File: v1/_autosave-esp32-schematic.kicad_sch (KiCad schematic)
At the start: 47 parts, among them J1 GN-2630G, J10 Screw_Terminal_01x04, J11 Screw_Terminal_01x04, J12 Screw_Terminal_01x04, J13 Screw_Terminal_01x04, J14 External Voltage Regulator, J15 POWER, J2 Jumper, J3 Micro_SD_Card, J4 Screw_Terminal_01x04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

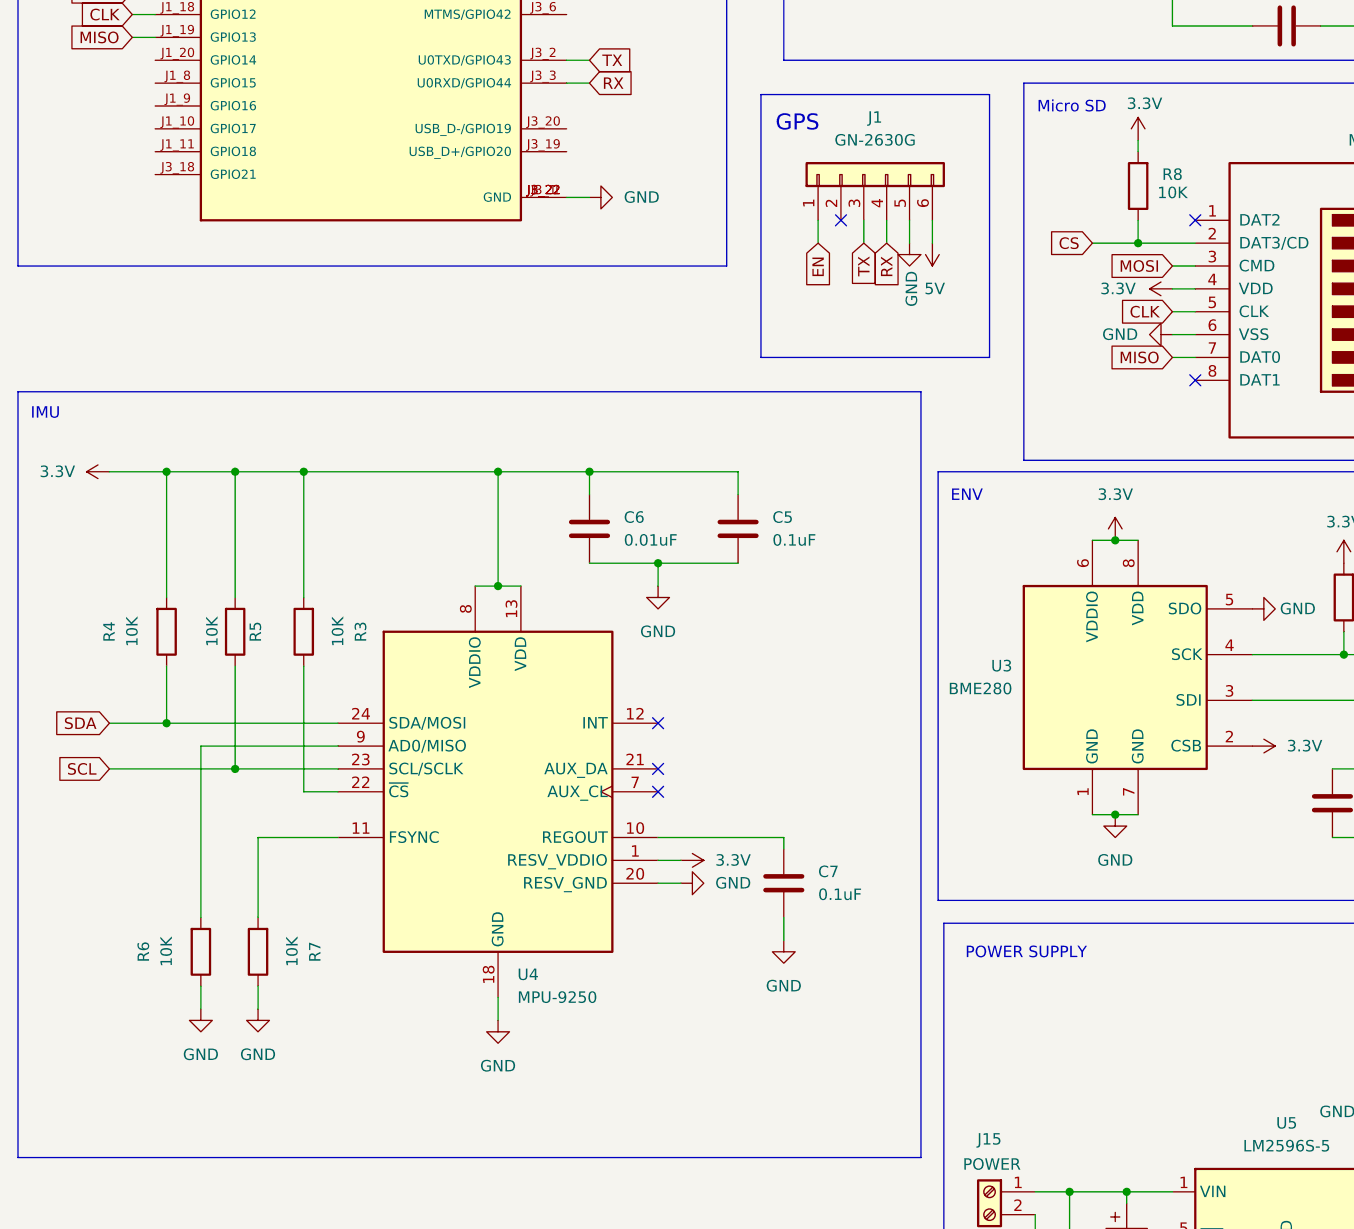
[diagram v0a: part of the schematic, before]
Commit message: index file added to identify the footprints of the components easily with a legible name
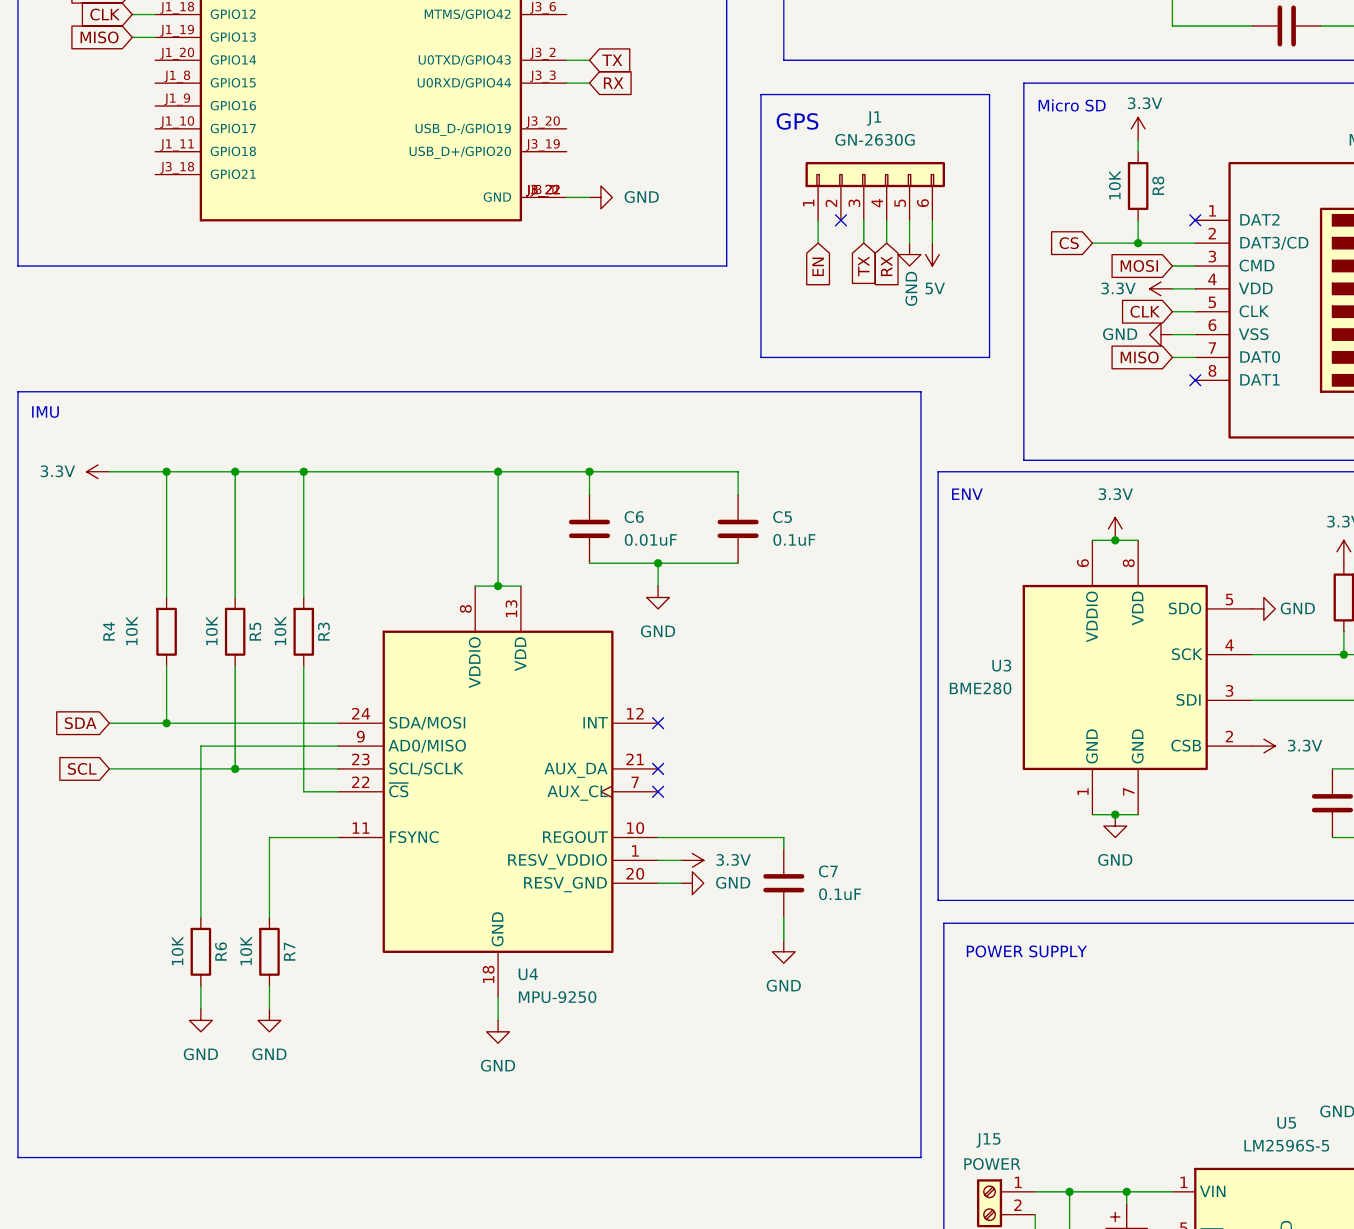
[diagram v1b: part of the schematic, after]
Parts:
- R3, R4, R5, R6, R7, R8: footprint Resistor_SMD:R_1206_3216Metric -> easyeda2kicad:R0603
